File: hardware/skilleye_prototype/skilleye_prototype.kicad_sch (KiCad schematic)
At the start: 0 parts

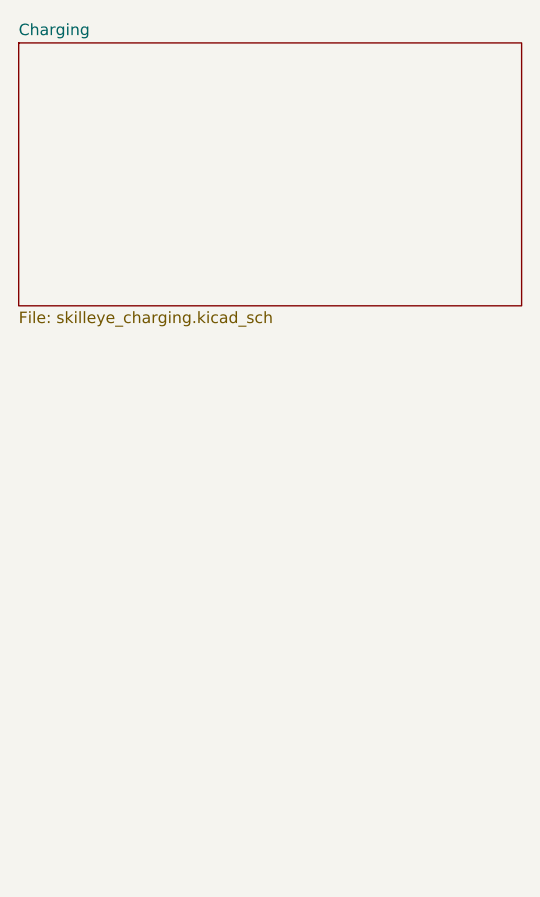
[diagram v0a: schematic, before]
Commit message: added regulator schematic + component libraries + datasheets
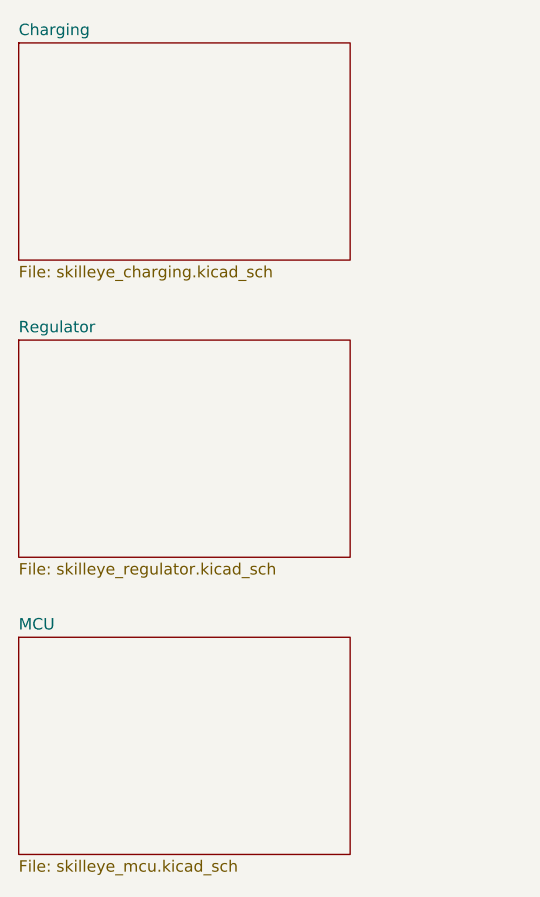
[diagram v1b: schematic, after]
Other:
- added sheet MCU (skilleye_mcu.kicad_sch)
- added sheet Regulator (skilleye_regulator.kicad_sch)
- company: (none) -> National Taipei University of Technology - Dept. of EECS
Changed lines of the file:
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@@
 	(generator_version "10.0")
 	(paper "A4")
+	(title_block
+		(company "National Taipei University of Technology - Dept. of EECS")
+		(comment 1 "SkillEye")
+		(comment 2 "Designer: Purit Hongjirakul")
+		(comment 3 "https://github.com/rizalfanex/SkillEye")
+	)
+	(sheet
+		(at 36.83 69.85)
+		(size 36.83 24.13)
+		(exclude_from_sim no)
+		(in_bom yes)
+		(on_board yes)
+		(dnp no)
+		(fields_autoplaced yes)
+		(stroke
+			(width 0.1524)
+			(type solid)
+		)
+		(fill
+			(color 0 0 0 0)
+		)
+		(property "Sheetname" "Regulator"
+			(at 36.83 69.1384 0)
+			(show_name no)
+			(do_not_autoplace no)
+			(effects
+				(font
+					(size 1.27 1.27)
+				)
+				(justify left bottom)
+			)
+		)
+		(property "Sheetfile" "skilleye_regulator.kicad_sch"
+			(at 36.83 94.5646 0)
+			(show_name no)
+			(do_not_autoplace no)
+			(effects
+				(font
+					(size 1.27 1.27)
+				)
+				(justify left top)
+			)
+		)
+		(instances
+			(project "skilleye_prototype"
+				(path "/e922ced9-cce7-4ffa-8992-2bb79546169b"
+					(page "3")
+				)
+			)
+		)
+	)
 	(sheet
 		(at 36.83 36.83)
-		(size 55.88 29.21)
+		(size 36.83 24.13)
 		(exclude_from_sim no)
 		(in_bom yes)
@@
 		)
 		(property "Sheetfile" "skilleye_charging.kicad_sch"
-			(at 36.83 66.6246 0)
+			(at 36.83 61.5446 0)
 			(show_name no)
 			(do_not_autoplace no)
@@
 				)
 			)
+		)
+	)
+	(sheet
+		(at 36.83 102.87)
+		(size 36.83 24.13)
+		(exclude_from_sim no)
+		(in_bom yes)
+		(on_board yes)
+		(dnp no)
+		(fields_autoplaced yes)
+		(stroke
+			(width 0.1524)
+			(type solid)
+		)
+		(fill
+			(color 0 0 0 0)
+		)
+		(property "Sheetname" "MCU"
+			(at 36.83 102.1584 0)
+			(show_name no)
+			(do_not_autoplace no)
+			(effects
+				(font
+					(size 1.27 1.27)
+				)
+				(justify left bottom)
+			)
+		)
+		(property "Sheetfile" "skilleye_mcu.kicad_sch"
+			(at 36.83 127.5846 0)
+			(show_name no)
+			(do_not_autoplace no)
+			(effects
+				(font
+					(size 1.27 1.27)
+				)
+				(justify left top)
+			)
+		)
+		(instances
+			(project "skilleye_prototype"
+				(path "/e922ced9-cce7-4ffa-8992-2bb79546169b"
+					(page "4")
+				)
+			)

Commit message: complete prototype rev1.0 schematics
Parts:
- added J2: USB_C_Receptacle_USB2.0_16P, symbol Connector:USB_C_Receptacle_USB2.0_16P
- added R11, R12: 5.1K, symbol Device:R
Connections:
- new net: J2.B5 (CC2), R11.1
- new net: J2.A5 (CC1), R12.1
- new net +5V: J2.A4 (VBUS), J2.A9 (VBUS), J2.B4 (VBUS), J2.B9 (VBUS)
- new net GND: J2.A1 (GND), J2.A12 (GND), J2.B1 (GND), J2.B12 (GND), J2.SH (SHIELD), R11.2, R12.2
- new net USB_DM: J2.A7 (D-), J2.B7 (D-)
- new net USB_DP: J2.A6 (D+), J2.B6 (D+)
- no-connect marks 0 -> 2
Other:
- title: (none) -> SkillEye
